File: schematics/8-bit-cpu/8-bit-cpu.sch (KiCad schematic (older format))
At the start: 0 parts

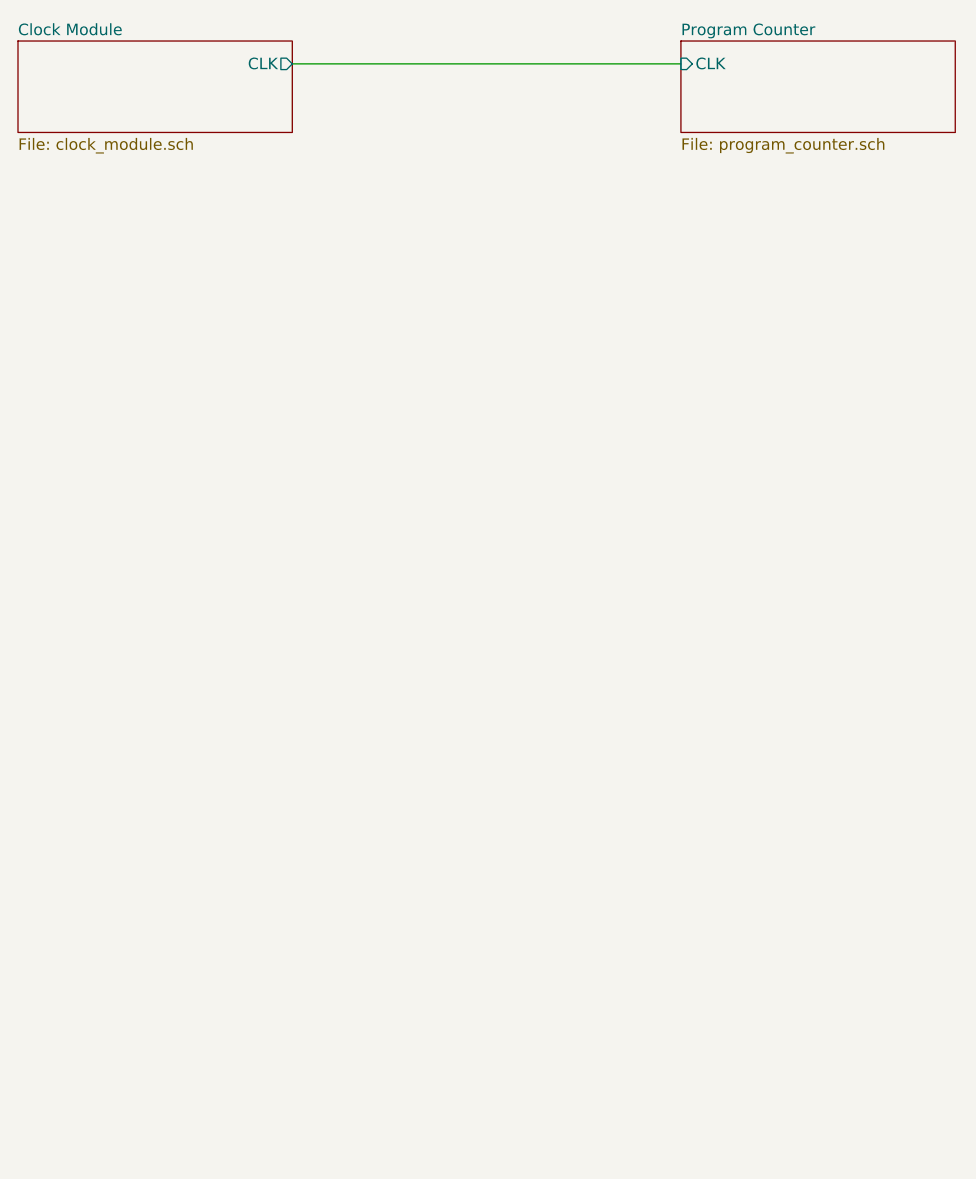
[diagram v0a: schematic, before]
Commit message: Added ALU, Accumulator and HL register schematics
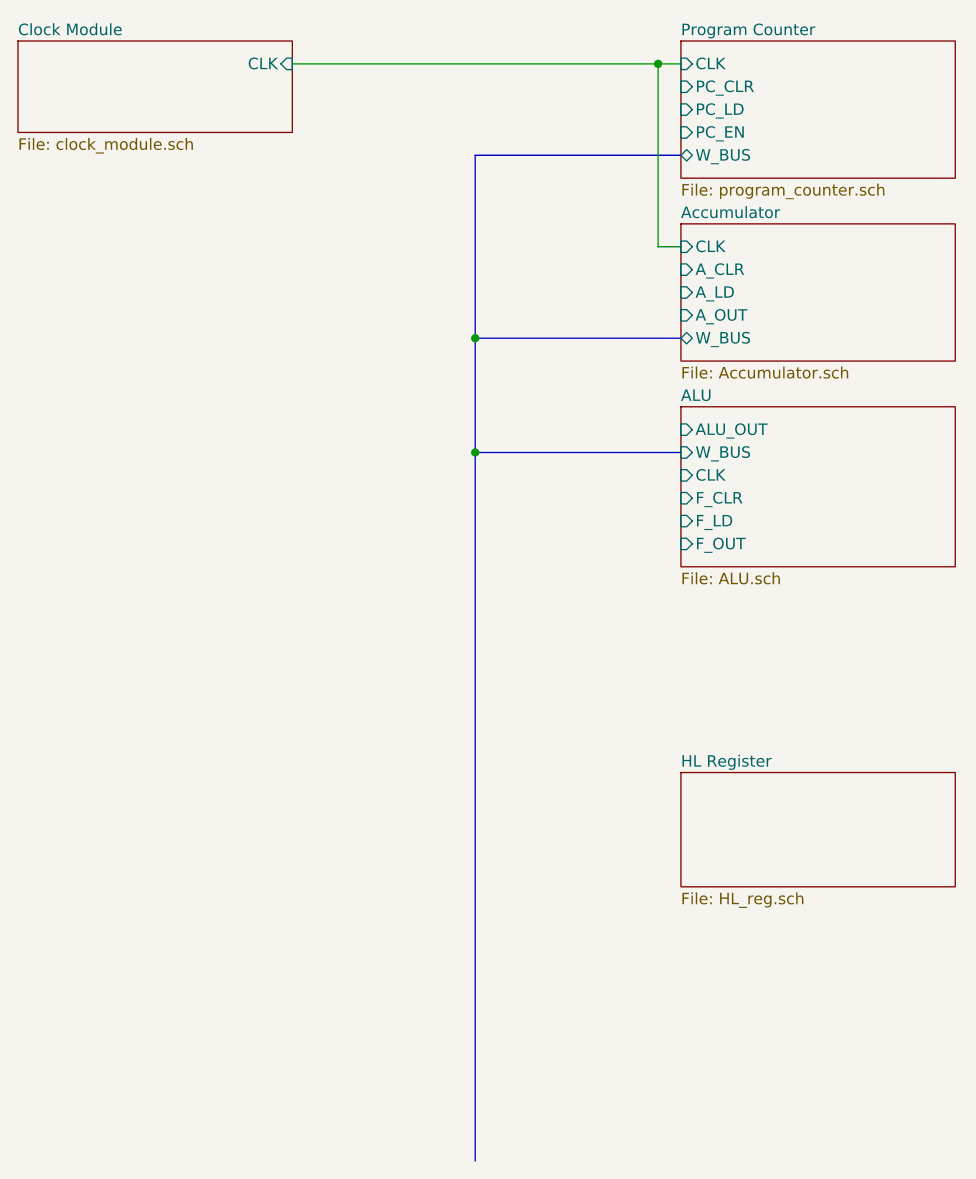
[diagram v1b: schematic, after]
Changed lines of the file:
@@
 EESchema Schematic File Version 4
 LIBS:8-bit-cpu-cache
-LIBS:Clock-cache
 EELAYER 26 0
 EELAYER END
 $Descr A4 8268 11693 portrait
 encoding utf-8
-Sheet 1 3
+Sheet 1 6
 Title ""
 Date ""
@@
 $EndDescr
 $Sheet
-S 4700 1200 1200 400
+S 4700 1200 1200 600
 U 5C212FAF
 F0 "Program Counter" 50
 F1 "program_counter.sch" 50
-F2 "CLK" I L 4700 1300 50
+F2 "W_BUS" B L 4700 1700 50
+F3 "CLK" I L 4700 1300 50
+F4 "PC_CLR" I L 4700 1400 50
+F5 "PC_LD" I L 4700 1500 50
+F6 "PC_EN" I L 4700 1600 50
 $EndSheet
 $Sheet
@@
 F0 "Clock Module" 50
 F1 "clock_module.sch" 50
-F2 "CLK" O R 3000 1300 50
+F2 "CLK" I R 3000 1300 50
 $EndSheet
 Wire Wire Line
-	3000 1300 4700 1300
+	3000 1300 4600 1300
+$Sheet
+S 4700 2000 1200 600
+U 5C2C69CB
+F0 "Accumulator" 50
+F1 "Accumulator.sch" 50
+F2 "CLK" I L 4700 2100 50
+F3 "A_CLR" I L 4700 2200 50
+F4 "A_LD" I L 4700 2300 50
+F5 "A_OUT" I L 4700 2400 50
+F6 "W_BUS" B L 4700 2500 50
+$EndSheet
+Wire Bus Line
+	3800 1700 3800 2500
+Wire Bus Line
+	4700 1700 3800 1700
+Wire Bus Line
+	4700 2500 3800 2500
+Connection ~ 3800 2500
+Wire Bus Line
+	3800 2500 3800 3000
+Wire Wire Line
+	4700 2100 4600 2100
+Wire Wire Line
+	4600 2100 4600 1300
+Connection ~ 4600 1300
+Wire Wire Line
+	4600 1300 4700 1300
+$Sheet
+S 4700 2800 1200 700
+U 5C2C9B12
+F0 "ALU" 50
+F1 "ALU.sch" 50
+F2 "ALU_OUT" I L 4700 2900 50
+F3 "W_BUS" I L 4700 3000 50
+F4 "CLK" I L 4700 3100 50
+F5 "F_CLR" I L 4700 3200 50
+F6 "F_LD" I L 4700 3300 50
+F7 "F_OUT" I L 4700 3400 50
+$EndSheet
+Wire Bus Line
+	4700 3000 3800 3000
+Connection ~ 3800 3000
+Wire Bus Line
+	3800 3000 3800 6100
+$Sheet
+S 4700 4400 1200 500
+U 5C2DD996
+F0 "HL Register" 50
+F1 "HL_reg.sch" 50
+$EndSheet
 $EndSCHEMATC
